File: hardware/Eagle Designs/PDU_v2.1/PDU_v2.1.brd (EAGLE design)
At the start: 90.2 x 95.5 mm, 265 parts, among them J1 5037630291, J10 5037630491, J11 UJ31-CH-G1-SMT-TR, J12 5037630291, J13 5037630291, J14 5037630291, J15 5037630291, J16 5037630291, J17 5037630291, J18 5037630491, J19 5037630291, J2 5037630291, J20 503182-1852, J22 5037630291, J23 5037630291, J24 5037630291, J25 5037630291, J27 5037630691, J3 5037630291, J4 5037630291, J5 5037630291, J6 5037630291, J7 5037630491, J8 5037630491, J9 5037630491, M1 BSZ100N06LS3, M2 BSZ100N06LS3, M3 BSZ033NE2LS5, M4 BSZ033NE2LS5, U1 DRV8847PWPR, U10 AO3404A, U11 IRLML2803PBFCT-ND, U12 IRLML2803PBFCT-ND, U13 LT8390EFE#PBF, U14 ATSAME51N19A-AF, U15 INA219BIDR, U16 MIC2514YM5-TR, U17 MAX16998AAUA+T, U18 TMP36FSZ, U2 DRV8847PWPR, U20 LTC4012IUFPBF, U21 LT8609A, U22 LT8609A, U23 BC848ALT1G, U24 AO3404A, U25 SI4835DDY-T1-GE3, U26 SI3493DDV-T1-GE3, U27 SI3493DDV-T1-GE3, U28 SI4431BDY-T1-E3, U29 AO4818B, U3 LTC1477CS8LINEAR_TECHNOLOGY_L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, U30 INA219BIDR, U31 INA219BIDR, U32 INA219BIDR, U33 INA219BIDR, U4 LTC1477CS8LINEAR_TECHNOLOGY_L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, U5 LTC1477CS8LINEAR_TECHNOLOGY_L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, U6 LTC1477CS8LINEAR_TECHNOLOGY_L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, U7 LTC1477CS8LINEAR_TECHNOLOGY_L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, U8 LT8609A, U9 LTC1477CS8LINEAR_TECHNOLOGY_L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, Y1 ABS07-32.768KHZ-T

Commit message: finalized OBC v4.20; updated PDU v2.1
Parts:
- added C65, C66, C67, C83, C89, C90: 0.1 uF, HSFL_Main_Library:0805
- added R91, R92, R93, R94, R95, R96: (no value), HSFL_Main_Library:0805
- added U19, U34, U35, U36, U37, U38: LND01K1-G, PDU:SOT-23-5_MC_MCH
- moved C14 40.9 mm to (64.2, 65.8), turned to 89.9 degrees
- moved D5 34.6 mm to (60.4, 65.8), turned to 270 degrees
- moved C_DC 30.8 mm to (37.1, 56.8)
- moved U28 29.6 mm to (32.3, 58.0), turned to 270 degrees
- moved C39 28.6 mm to (56.8, 65.9), turned to 90 degrees
- moved R39 13.9 mm to (63.6, 60.1), turned to 270 degrees
- moved R53 13.8 mm to (60.8, 60.1), turned to 90 degrees
- moved R35 13.5 mm to (57.9, 60.1)
- moved C29 13.4 mm to (54.9, 60.2)
- moved R90 10.9 mm to (68.3, 55.5)
- moved R85 9.99 mm to (68.4, 58.5)
- moved C42 9.25 mm to (58.8, 68.1)
- moved R81 8.95 mm to (55.7, 68.9)
- moved R62 8.77 mm to (64.6, 71.3), turned to 180 degrees
- moved R89 7.88 mm to (57.4, 68.0)
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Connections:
- new net N$32: R91.1, U19.4
- new net N$35: R92.1, U34.4
- new net N$60: R93.1, U35.4
- new net N$62: R94.1, U36.4
- new net N$72: R95.1, U37.4
- new net N$74: R96.1, U38.4
- net BUS_3V3: now also C65.1, C66.1
- net BUS_5V: now also C67.1, C83.1, C89.1, C90.1
- net GND: now also C65.2, C66.2, C67.2, C83.2, C89.2, C90.2, R91.2, R92.2, R93.2, R94.2, R95.2, R96.2
- net SW_3V3_1: now also U19.5
- net SW_3V3_2: now also U34.5
- net SW_3V3_EN1: now also U19.2
- net SW_3V3_EN2: now also U34.2
- net SW_5V_1: now also U35.5
- net SW_5V_2: now also U36.5
- net SW_5V_3: now also U37.5
- net SW_5V_4: now also U38.5
- net SW_5V_EN1: now also U35.2
- net SW_5V_EN2: now also U36.2
- net SW_5V_EN3: now also U37.2
- net SW_5V_EN4: now also U38.2
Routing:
- net BUS_3V3: track 281.1 -> 360.8 mm
- net AIN6: track 72.1 -> 47.7 mm
- net U2_S: track 0.00 -> 21.3 mm
- net CS_VBATT_VIN-: track 0.00 -> 18.0 mm
- net I2C1_SCL: track 0.00 -> 17.7 mm
- net I2C1_SDA: track 0.00 -> 17.0 mm
- net BUS_5V: track 306.8 -> 323.1 mm
- net BATT_CHRG: track 135.3 -> 150.6 mm
- net N$51: track 0.00 -> 15.3 mm
- net N$37: track 0.00 -> 14.8 mm
- net N$56: track 0.00 -> 14.3 mm
- net N$54: track 0.00 -> 12.8 mm
- net VBATT: track 218.2 -> 231.0 mm
- net N$53: track 0.00 -> 11.7 mm
- net CS_SOL2_VIN-: track 0.00 -> 11.6 mm
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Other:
- board text removed: "C:/Users/kelly/Downloads/official.bmp"

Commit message: updated PDU v2.1 (ongoing board cleanup)
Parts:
- removed R91, R92, R94, R95, R96: (no value), HSFL_Main_Library:0805
- removed U19, U34, U36, U37, U38: LND01K1-G, PDU:SOT-23-5_MC_MCH
- moved R93 140.4 mm to (18.4, 65.2), flipped to the bottom, turned to 270 degrees
- moved U35 112.2 mm to (20.3, 69.4), flipped to the bottom
- moved NT1 17.7 mm to (9.64, 39.0), turned to 0 degrees
- moved R81 10.4 mm to (66.1, 69.7)
- moved C42 10.3 mm to (69.0, 69.8)
- moved C83 9.83 mm to (57.8, 78.2), flipped to the bottom, turned to 90 degrees
- moved R88 8.17 mm to (65.6, 65.4)
- moved R57 7.40 mm to (17.2, 61.3), turned to 0 degrees
- moved C11 6.55 mm to (16.2, 69.4)
- moved R90 6.34 mm to (64.7, 60.7), turned to 90 degrees
- moved C13 5.87 mm to (40.2, 57.8), turned to 180 degrees
- moved R89 5.86 mm to (63.0, 69.6), turned to 270 degrees
- moved U7 5.06 mm to (55.6, 70.6)
- moved C15 4.74 mm to (46.0, 71.9), turned to 270 degrees
- moved R_SENSE 4.59 mm to (45.3, 70.7), turned to 180 degrees
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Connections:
- removed net N$32: R91.1, U19.4
- removed net N$35: R92.1, U34.4
- removed net N$62: R94.1, U36.4
- removed net N$72: R95.1, U37.4
- removed net N$74: R96.1, U38.4
- net GND: no longer R91.2, R92.2, R94.2, R95.2, R96.2
- net SD_CS: now also H1.2.49, J20.2; no longer J20.1
- net SD_MISO: now also H1.2.52
- net SD_MOSI: now also H1.2.51
- net SD_SCK: now also H1.2.50
- net SW_3V3_1: no longer U19.5
- net SW_3V3_2: no longer U34.5
- net SW_3V3_EN1: no longer U19.2
- net SW_3V3_EN2: no longer U34.2
- net SW_5V_2: no longer U36.5
- net SW_5V_3: no longer U37.5
- net SW_5V_4: no longer U38.5
- net SW_5V_EN2: no longer U36.2
- net SW_5V_EN3: no longer U37.2
- net SW_5V_EN4: no longer U38.2
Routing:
- net BUS_3V3: track 360.8 -> 473.1 mm, vias 14 -> 18
- net SOLAR_IN2: track 1.58 -> 93.3 mm, vias 0 -> 2
- net VBATT: track 231.0 -> 321.7 mm, vias 6 -> 10
- net SOLAR_IN3_LOAD: track 0.00 -> 89.3 mm, vias 0 -> 2
- net UART2_TXD: track 64.0 -> 151.1 mm, vias 1 -> 2
- net UART2_RXD: track 59.0 -> 142.0 mm, vias 1 -> 2
- net SOLAR_IN3: track 7.03 -> 87.5 mm, vias 1 -> 2
- net I2C1_SDA: track 17.0 -> 96.1 mm, vias 0 -> 4
- net SOLAR_IN2_LOAD: track 6.01 -> 79.4 mm, vias 0 -> 4
- net I2C1_SCL: track 17.7 -> 89.0 mm, vias 0 -> 4
- net SD_SCK: track 47.0 -> 111.4 mm
- net SD_MISO: track 56.5 -> 117.7 mm
- net SOLAR_IN1_LOAD: track 10.3 -> 70.6 mm, vias 0 -> 4
- net BUS_5V: track 323.1 -> 382.7 mm, vias 7 -> 10
- net CS_VBATT: track 2.92 -> 62.3 mm, vias 0 -> 2
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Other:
- board text added: "CS SP1"
- board text added: "CS SPI2"
- board text added: "MCU LED"
- board text removed: "BATT BRD"
- board text removed: "CURR SENS"
- board text removed: "LED"
- board text removed: "SOL CHRG"

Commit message: completed PDU v2.1 (awaiting feedback)
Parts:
- moved R90 9.01 mm to (56.0, 63.0)
- moved R84 7.86 mm to (59.8, 63.0)
- moved R76 7.66 mm to (83.1, 64.8)
- moved C61 7.39 mm to (63.1, 62.9)
- moved C71 6.99 mm to (83.3, 53.4)
- moved C11 5.82 mm to (15.9, 75.2), turned to 90 degrees
- moved U33 5.43 mm to (70.5, 61.7)
- moved R81 4.42 mm to (62.1, 71.6)
- moved U16 4.30 mm to (58.0, 56.0)
- moved R36 4.27 mm to (83.3, 61.0)
- moved C42 3.88 mm to (65.6, 71.7)
- moved R89 3.61 mm to (59.9, 67.8), turned to 90 degrees
- moved U32 3.39 mm to (72.5, 69.6)
- moved R78 3.31 mm to (83.2, 57.0)
- moved R85 3.25 mm to (64.4, 58.1)
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- renumbered C_DC to C91, LED1 to D13, R_CL to R91, R_F to R96, R_IN1 to R92, R_IN2 to R94, R_SENSE to R95
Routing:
- net I2C1_SDA: track 96.1 -> 116.8 mm, vias 4 -> 5
- net BUS_3V3: track 473.1 -> 491.8 mm
- net SOLAR_IN4: track 60.5 -> 70.8 mm
- net SOLAR_IN4_LOAD: track 56.4 -> 66.4 mm
- net GND: track 78.7 -> 85.5 mm, vias 21 -> 24
- net SW_VBATT_EN: track 25.1 -> 31.1 mm
- net SW_VBATT: track 54.5 -> 59.1 mm
- net SW_5V_1: track 29.9 -> 33.9 mm
- net INH_SW1_COM: track 287.4 -> 291.3 mm
- net VDD: track 111.5 -> 114.9 mm
- net CS_SOL4_VIN-: track 6.67 -> 9.88 mm
- net BUS_5V: track 382.7 -> 385.6 mm
- net RBF_SW: track 11.6 -> 13.8 mm
- net CS_SOL4_VIN+: track 6.21 -> 8.40 mm
- net SOLAR_IN3_LOAD: track 89.3 -> 87.4 mm
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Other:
- board text added: "CS BATT"
- board text added: "CS SP3"
- board text added: "CS SP4"
- board text added: "Dep. MOSFET"
- board text added: "MCU"
- board text added: "RBF"
- board text added: "U35"
- board text removed: "Filter"
- board text removed: "Heater"
- board text removed: "Microprocessor"
- board text removed: "RBF Circuit"

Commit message: finalized PDU v2.1 and generated Gerber Files
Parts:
- added C92: 1 uF, HSFL_Main_Library:1206
- added R97: 16, HSFL_Main_Library:0805
- C44: value 1uF -> 1 uF
- R93: value (none) -> 10 k
- moved R58 4.79 mm to (18.7, 54.8), turned to 270 degrees
- moved C22 1.82 mm to (28.0, 52.7)
- moved U24 1.43 mm to (9.29, 54.4)
- moved R82 1.12 mm to (9.50, 51.2)
- moved C73 0.86 mm to (27.9, 56.9)
- moved C26 0.59 mm to (14.8, 52.1)
- moved U17 0.59 mm to (23.4, 60.9)
- moved C5 0.51 mm to (22.0, 48.9)
- moved D10 0.46 mm to (82.4, 45.0)
- moved R16 0.46 mm to (22.0, 51.9)
- moved J5 0.46 mm to (81.2, 50.0)
- moved J16 0.42 mm to (12.6, 64.0)
- moved R57 0.33 mm to (16.9, 61.4)
- moved C25 0.28 mm to (15.2, 49.3)
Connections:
- new net POST_RBF_VBATT: R97.1, U24.2
- net CS_VBATT: now also C92.1, R97.2; no longer U24.2
- net GND: now also C92.2
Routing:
- net CS_VBATT: track 62.0 -> 71.4 mm
- net PY_VBATT: track 34.1 -> 41.2 mm
- net POST_RBF_VBATT: track 0.00 -> 3.02 mm
- net VBATT: track 321.5 -> 323.5 mm
- net N$20: track 6.65 -> 5.07 mm
- net UART2_TXD: track 151.1 -> 151.8 mm
- net WDT_WDI: track 47.3 -> 46.7 mm
- net N$70: track 10.0 -> 10.7 mm
- net N$66: track 5.12 -> 4.48 mm
- net SW_5V_3: track 100.7 -> 101.3 mm
- net BUS_3V3_TRSS: track 5.07 -> 4.53 mm
- net WDT_EN: track 3.36 -> 3.89 mm
- net GND: track 85.5 -> 85.6 mm, vias 24 -> 25

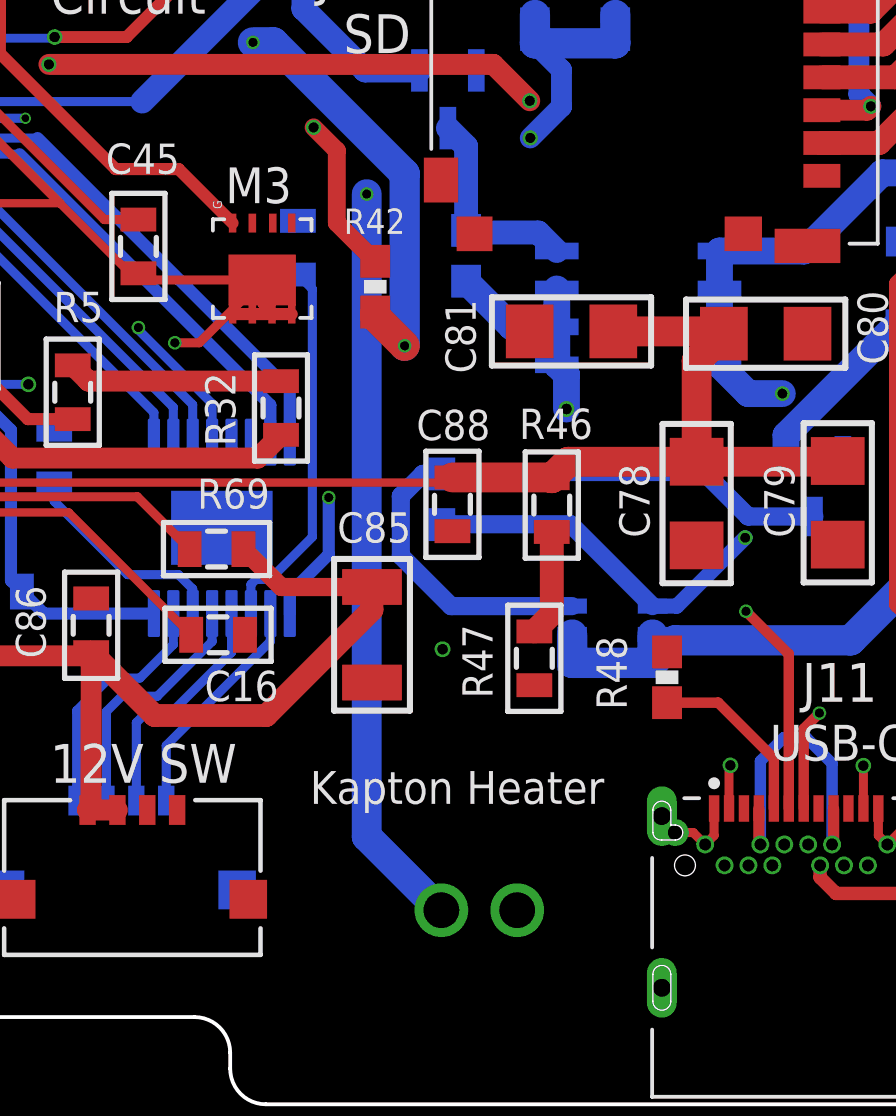
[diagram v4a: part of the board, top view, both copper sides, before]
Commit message: added Kapton Heater Connector (device) to PDU v2.1
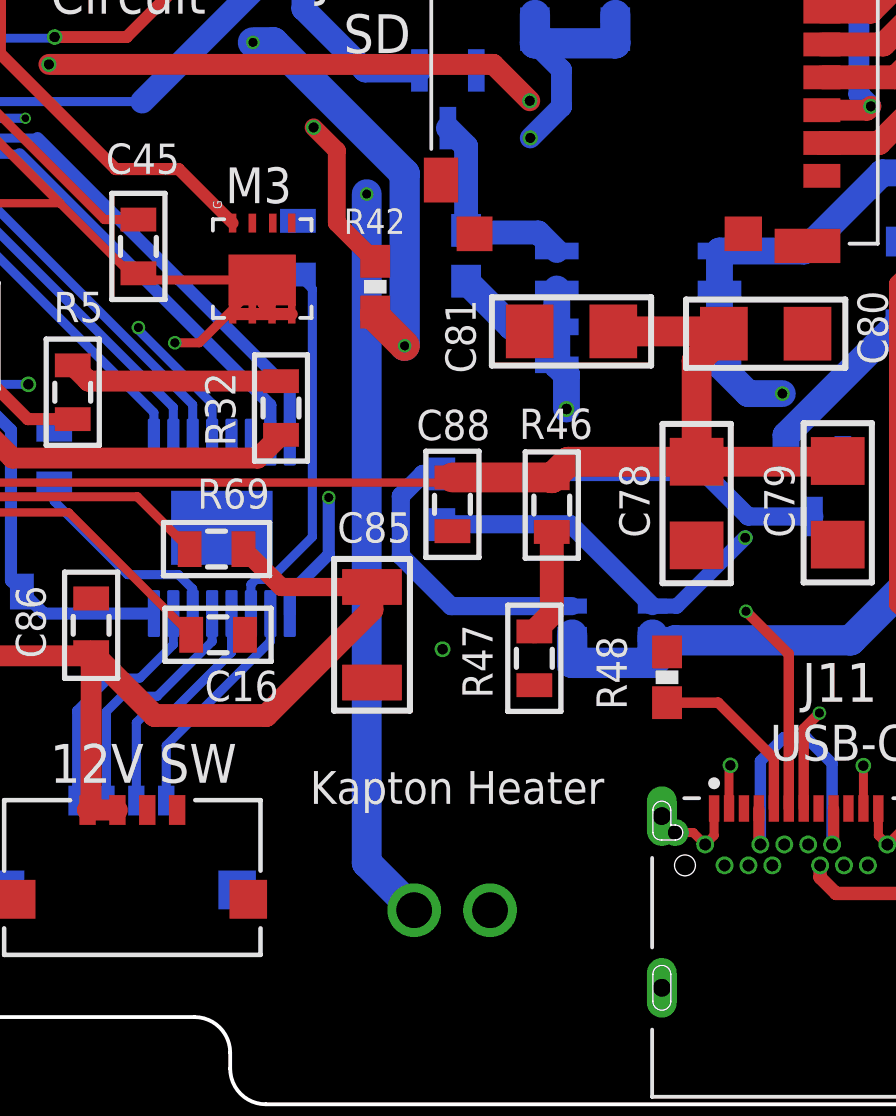
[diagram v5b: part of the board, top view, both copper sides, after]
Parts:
- added J28: 68016-202HLF, PDU:68016-202HLF
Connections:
- net GND: now also J28.2
- net SW_5V_2: now also J28.1
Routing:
- net SW_5V_2: track 119.3 -> 118.9 mm, vias 6 -> 5
- net GND: vias 25 -> 24
